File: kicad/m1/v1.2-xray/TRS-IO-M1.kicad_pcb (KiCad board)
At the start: 2 copper layers, 111.9 x 94 mm, 32 parts, among them J1 Conn_02x20_Odd_Even, J2 Conn_02x20_Odd_Even, J3 SD_Card, J4 Conn_01x02_Male, J5 Conn_01x02_Male, Q1 2N7000, Q2 2N7000, SW1 SW_Push, U1 HiLetgo-ESP-32S, U2 Artix-7-15T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

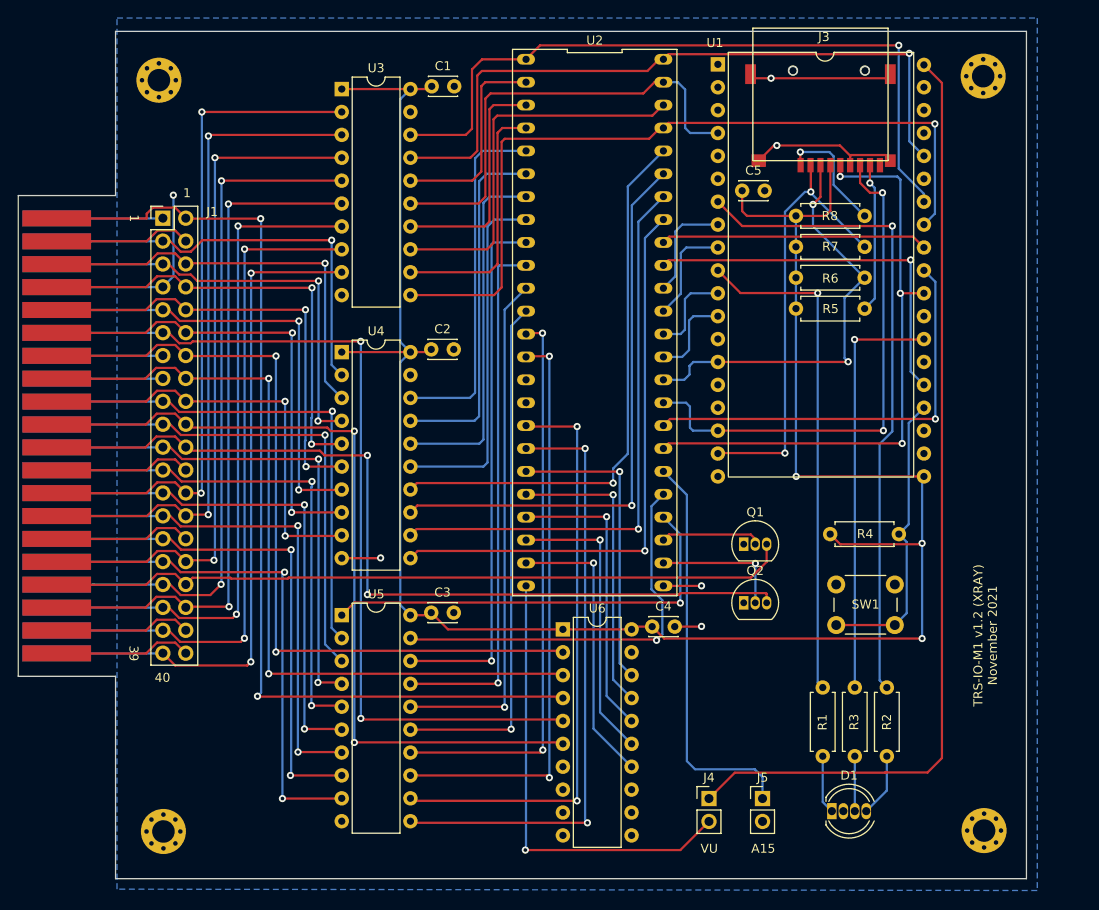
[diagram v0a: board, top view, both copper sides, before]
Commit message: Update TRS-IO-XRAY to KiCad 6
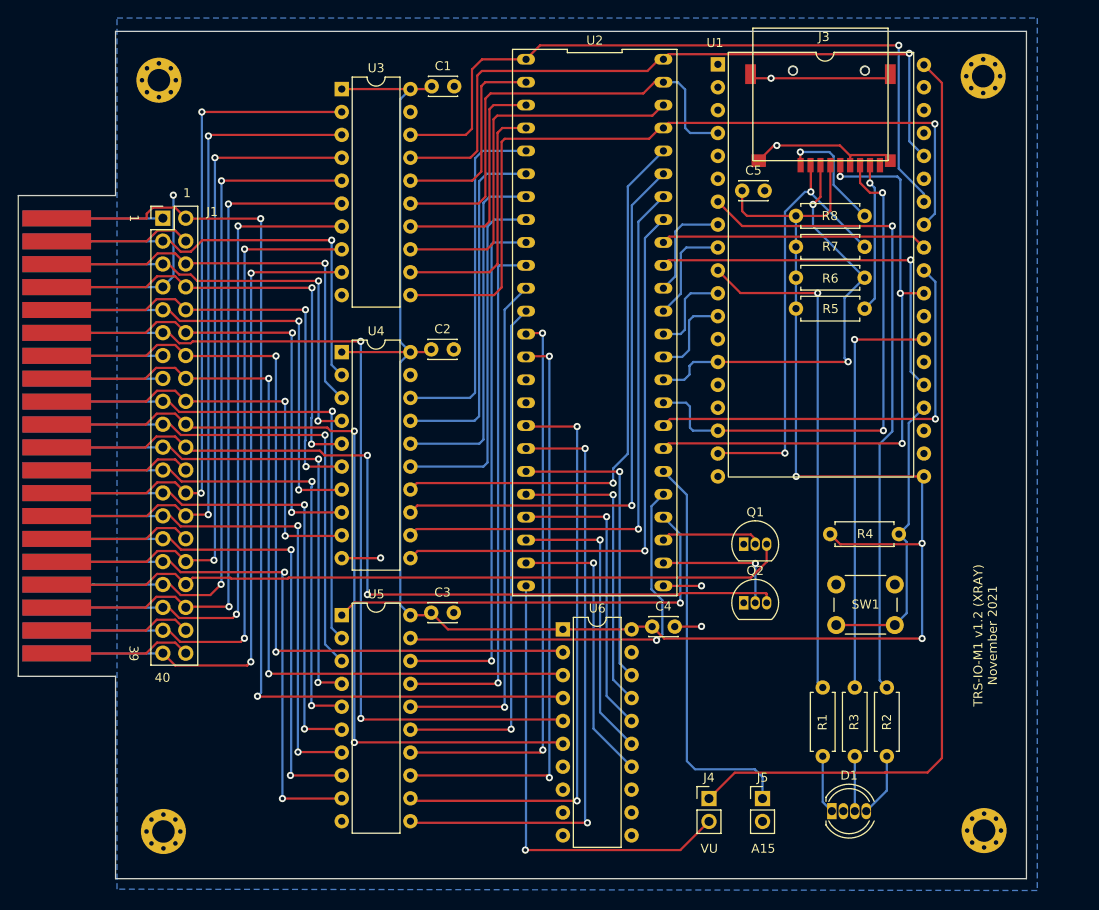
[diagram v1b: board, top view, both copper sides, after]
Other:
- net class Default removed
- net class Power removed

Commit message: Add VGA to TRS-IO-XRAY schematics and PCB
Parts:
- added J6: DB15_Female_HighDensity, TRS-IO-M1:DB_15F-VGA, F.Cu at (213.4, 115.2)
- added U7: MCP43x1, Package_SO:TSSOP-20_4.4x6.5mm_P0.65mm, F.Cu at (191.9, 72.1)
- moved J4 72.0 mm to (207.2, 66.8), turned to 180 degrees
- moved J5 71.4 mm to (211.5, 66.8), turned to 180 degrees
- moved SW1 28.6 mm to (184.4, 136.6), turned to 180 degrees
- moved R5 12.2 mm to (187.9, 90.9)
- moved R6 12.2 mm to (187.9, 87.5)
- moved R7 12.2 mm to (187.9, 84.0)
- moved R8 12.2 mm to (187.9, 80.6)
- moved C5 4.09 mm to (187.2, 65.5), turned to 180 degrees
- turned U2 to 90 degrees
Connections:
- J3 pad 9: Net-(J3-Pad9) -> unconnected-(J3-Pad9)
- U1 pad 1: Net-(U1-Pad1) -> unconnected-(U1-Pad1)
- U1 pad 12: ESP_S3 -> CS_MCP43x1
- U1 pad 15: Net-(U1-Pad15) -> unconnected-(U1-Pad15)
- U1 pad 16: Net-(U1-Pad16) -> unconnected-(U1-Pad16)
- U1 pad 2: Net-(U1-Pad2) -> unconnected-(U1-Pad2)
- U1 pad 21: Net-(U1-Pad21) -> unconnected-(U1-Pad21)
- U1 pad 22: Net-(U1-Pad22) -> unconnected-(U1-Pad22)
- U1 pad 25: Net-(U1-Pad25) -> unconnected-(U1-Pad25)
- U1 pad 27: Net-(U1-Pad27) -> FULL_ADDR
- U1 pad 3: Net-(U1-Pad3) -> unconnected-(U1-Pad3)
- U1 pad 35: Net-(U1-Pad35) -> unconnected-(U1-Pad35)
- U1 pad 36: Net-(U1-Pad36) -> unconnected-(U1-Pad36)
- U1 pad 37: Net-(U1-Pad37) -> unconnected-(U1-Pad37)
- U1 pad 5: Net-(U1-Pad5) -> unconnected-(U1-Pad5)
- U1 pad 6: Net-(U1-Pad6) -> unconnected-(U1-Pad6)
- U2 pad 1: AA0 -> INT
- U2 pad 10: DD7 -> ESP_S1
- U2 pad 11: DD1 -> ESP_S0
- U2 pad 12: DD6 -> REQ
- U2 pad 13: DD3 -> DONE
- U2 pad 14: DD5 -> AA9
- U2 pad 15: Net-(U2-Pad15) -> unconnected-(U2-Pad15)
- U2 pad 16: Net-(U2-Pad16) -> unconnected-(U2-Pad16)
- U2 pad 17: DD0 -> AA8
- U2 pad 18: DD2 -> AA14
- U2 pad 19: Z80_WR_N -> AA11
- U2 pad 2: AA4 -> VGA_VSYNC
- U2 pad 20: Z80_RD_N -> AA2
- U2 pad 21: Z80_RAS_N -> AA7
- U2 pad 22: Z80_OUT_N -> AA3
- U2 pad 23: Z80_IN_N -> AA1
- U2 pad 26: INT -> AA0
- U2 pad 27: WAIT -> AA4
- U2 pad 28: READ_N -> AA5
- U2 pad 29: DBUS_SEL_N -> AA6
- U2 pad 3: AA5 -> VGA_HSYNC
- U2 pad 30: FULL_ADDR -> AA10
- U2 pad 31: SCK -> AA12
- U2 pad 32: CS_FPGA -> AA13
- U2 pad 33: MISO -> AA15
- U2 pad 34: MOSI -> DD4
- U2 pad 35: ESP_S3 -> DD7
- U2 pad 36: ESP_S2 -> DD1
- U2 pad 37: ESP_S1 -> DD6
- U2 pad 38: ESP_S0 -> DD3
- U2 pad 39: REQ -> DD5
- U2 pad 4: AA6 -> SCK
- U2 pad 40: DONE -> DD0
- U2 pad 41: AA9 -> DD2
- U2 pad 42: AA8 -> Z80_WR_N
- U2 pad 43: AA14 -> Z80_RD_N
- U2 pad 44: AA11 -> Z80_OUT_N
- U2 pad 45: AA2 -> Z80_IN_N
- U2 pad 46: AA7 -> WAIT
- U2 pad 47: AA3 -> READ_N
- U2 pad 48: AA1 -> DBUS_SEL_N
- U2 pad 5: AA10 -> CS_FPGA
- U2 pad 6: AA12 -> MISO
- U2 pad 7: AA13 -> MOSI
- U2 pad 8: AA15 -> VGA_RGB
- U2 pad 9: DD4 -> ESP_S2
- U6 pad 11: Net-(U6-Pad11) -> unconnected-(U6-Pad11)
- U6 pad 12: Net-(U6-Pad12) -> unconnected-(U6-Pad12)
- U6 pad 13: Net-(U6-Pad13) -> unconnected-(U6-Pad13)
- U6 pad 7: Net-(U6-Pad7) -> unconnected-(U6-Pad7)
- U6 pad 8: Net-(U6-Pad8) -> unconnected-(U6-Pad8)
- U6 pad 9: Net-(U6-Pad9) -> unconnected-(U6-Pad9)
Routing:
- net +5V: track 105.6 -> 17.6 mm
- net POT_VGA_GREEN: track 0.00 -> 62.2 mm, vias 0 -> 1
- net VGA_RGB: track 0.00 -> 56.4 mm, vias 0 -> 7
- net POT_VGA_BLUE: track 0.00 -> 54.4 mm, vias 0 -> 1
- net POT_VGA_RED: track 0.00 -> 53.4 mm, vias 0 -> 1
- net VGA_VSYNC: track 0.00 -> 47.4 mm, vias 0 -> 1
- net VGA_HSYNC: track 0.00 -> 46.5 mm, vias 0 -> 1
- net BUTTON: track 32.7 -> 66.0 mm, vias 0 -> 1
- net Z80_RAS_N: track 32.8 -> 0.00 mm, vias 1 -> 0
- net DBUS_SEL_N: track 44.9 -> 18.7 mm
- net FULL_ADDR: track 44.7 -> 20.7 mm
- net CS_MCP43x1: track 0.00 -> 23.3 mm, vias 0 -> 2
- net READ_N: track 48.5 -> 25.8 mm
- net GND: track 97.6 -> 120.3 mm, vias 6 -> 11
- net Net-(J3-Pad8): track 16.6 -> 34.1 mm
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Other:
- board text added: "TRS-IO-M1 v1.2 (XRAY) January 2022"
- board text removed: "TRS-IO-M1 v1.2 (XRAY) November 2021"
